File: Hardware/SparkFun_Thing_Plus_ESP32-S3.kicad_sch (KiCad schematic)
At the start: 35 parts, among them J1 USB_C_Receptacle, SW1 4.6x2.8mm, SW2 4.6x2.8mm, U10 ThingPlus, U2 TVS_ESD_USB, U3 ESP32-S3-MINI, U6 AP2112K-3.3

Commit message: Update rev number
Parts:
- R7: PROD_ID RES-14883 -> RES-15187
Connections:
- net +3.3V renamed 3.3V
- net +5V renamed 5V

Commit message: Updates post review
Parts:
- U6: value AP2112K-3.3 -> RT9080-3.3; symbol SparkFun-Regulator:AP2112K-3.3 -> SparkFun-Regulator:RT9080-3.3; Imax (none) -> 600mA; Iq (none) -> 4µA; PROD_ID VREG-12457 -> VREG-19034; VMax (none) -> 6V
- renumbered JP4 to PWR1
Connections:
- net ESP35/~{ALRT}: now reaches U3.31 (IO35)
- net 5V renamed VIN
- net ESP41/NC renamed ESP41/LP_CTL
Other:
- note added: "Differential Pair Calculation Copper Thickness (1oz): 1.4mil/0.035mm Board thickness: 1.6mm Dielectric thickness (layer 1 to 2): 7.9mil/0.2mm Er: 4.6 Trace Spacing: 6mil/0.1524mm Required Trace Width: 9mil/0.2286mm Source: Saturn PCB Toolkit"
- note added: "For modules with ordering codes ending with -N4R2, IO26 connects to the embedded PSRAM and is not available for other uses."
- note added: "IO3: JTAG Signal Source. GPIO by default."
- note removed: "In module variants that have embedded OSPI PSRAM, i.e., that embed ESP32-S3R8, pins IO35, IO36, and IO37 connect to the OSPI PSRAM and are not available for other uses."
- moved on the sheet: C1, C3, C7, D1, R1, R7, SW1, SW2, TP2

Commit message: Add default on to Qwiic power.
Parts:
- JP1: renamed from PWR1; value ~ -> PWR
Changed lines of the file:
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@@
   (symbol (lib_id "SparkFun-Jumper:SolderJumper_2_Bridged") (at 186.69 34.29 90) (unit 1)
     (in_bom yes) (on_board yes) (dnp no) (fields_autoplaced)
-    (property "Reference" "PWR1" (at 184.658 34.29 0)
+    (property "Reference" "JP1" (at 184.658 34.29 0)
       (effects (font (size 1.27 1.27)))
     )
-    (property "Value" "~" (at 189.23 34.29 0)
+    (property "Value" "PWR" (at 189.23 34.29 0)
       (effects (font (size 1.27 1.27)))
     )
@@
       (project "SparkFun_Thing_Plus_ESP32-S3"
         (path "/e3dd3ae4-244d-4cba-9cca-5d2abf83f29a"
-          (reference "PWR1") (unit 1)
+          (reference "JP1") (unit 1)
         )
       )

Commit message: Revise layout post design review
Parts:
- C10: value 1.0uF -> 2.2uF; symbol SparkFun-Capacitor:1.0uF_0402_16V_10% -> SparkFun-Capacitor:2.2uF_0402_10V_10%; PROD_ID CAP-14969 -> CAP-14232; Voltage 16V -> 10V
- SW1, SW2: footprint SparkFun-Switch:Momentary_SMD_4.6x2.8mm -> SparkFun-Switch:Momentary_SMD_4.6x2.8mm_h2.5mm; symbol SparkFun-Switch:SPST_Momentary_4.6x2.8mm -> SparkFun-Switch:SPST_Momentary_SMD_4.6x2.8mm_h2.5mm
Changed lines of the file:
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@@
     )
   )
-  (symbol (lib_id "SparkFun-Switch:SPST_Momentary_4.6x2.8mm") (at 36.83 101.6 270) (unit 1)
+  (symbol (lib_id "SparkFun-Switch:SPST_Momentary_SMD_4.6x2.8mm_h2.5mm") (at 36.83 101.6 270) (unit 1)
     (in_bom yes) (on_board yes) (dnp no) (fields_autoplaced)
     (property "Reference" "SW1" (at 39.37 100.33 90)
@@
       (effects (font (size 1.27 1.27)) (justify left))
     )
-    (property "Footprint" "SparkFun-Switch:Momentary_SMD_4.6x2.8mm" (at 31.75 101.6 0)
-      (effects (font (size 1.27 1.27)) hide)
-    )
-    (property "Datasheet" "~" (at 36.83 101.6 0)
+    (property "Footprint" "SparkFun-Switch:Momentary_SMD_4.6x2.8mm_h2.5mm" (at 31.75 101.6 0)
+      (effects (font (size 1.27 1.27)) hide)
+    )
+    (property "Datasheet" "~" (at 26.67 101.6 0)
       (effects (font (size 1.27 1.27)) hide)
     )
@@
     )
   )
-  (symbol (lib_id "SparkFun-Capacitor:1.0uF_0402_16V_10%") (at 133.35 52.07 0) (unit 1)
+  (symbol (lib_id "SparkFun-Capacitor:2.2uF_0402_10V_10%") (at 133.35 52.07 0) (unit 1)
     (in_bom yes) (on_board yes) (dnp no) (fields_autoplaced)
     (property "Reference" "C10" (at 137.16 48.26 0)
       (effects (font (size 1.27 1.27)) (justify left))
     )
-    (property "Value" "1.0uF" (at 137.16 50.8 0)
+    (property "Value" "2.2uF" (at 137.16 50.8 0)
       (effects (font (size 1.27 1.27)) (justify left))
     )
@@
       (effects (font (size 1.27 1.27)) hide)
     )
-    (property "Datasheet" "https://cdn.sparkfun.com/assets/8/a/4/a/5/Kemet_Capacitor_Datasheet.pdf" (at 133.35 66.04 0)
-      (effects (font (size 1.27 1.27)) hide)
-    )
-    (property "PROD_ID" "CAP-14969" (at 132.08 68.58 0)
-      (effects (font (size 1.27 1.27)) hide)
-    )
-    (property "Voltage" "16V" (at 137.16 53.34 0)
+    (property "Datasheet" "https://cdn.sparkfun.com/assets/8/a/4/a/5/Kemet_Capacitor_Datasheet.pdf" (at 134.62 68.58 0)
+      (effects (font (size 1.27 1.27)) hide)
+    )
+    (property "PROD_ID" "CAP-14232" (at 132.08 66.04 0)
+      (effects (font (size 1.27 1.27)) hide)
+    )
+    (property "Voltage" "10V" (at 137.16 53.34 0)
       (effects (font (size 1.27 1.27)) (justify left))
     )
@@
     )
   )
-  (symbol (lib_id "SparkFun-Switch:SPST_Momentary_4.6x2.8mm") (at 35.56 148.59 270) (unit 1)
+  (symbol (lib_id "SparkFun-Switch:SPST_Momentary_SMD_4.6x2.8mm_h2.5mm") (at 35.56 148.59 270) (unit 1)
     (in_bom yes) (on_board yes) (dnp no) (fields_autoplaced)
     (property "Reference" "SW2" (at 38.1 147.32 90)
@@
       (effects (font (size 1.27 1.27)) (justify left))
     )
-    (property "Footprint" "SparkFun-Switch:Momentary_SMD_4.6x2.8mm" (at 30.48 148.59 0)
-      (effects (font (size 1.27 1.27)) hide)
-    )
-    (property "Datasheet" "~" (at 35.56 148.59 0)
-      (effects (font (size 1.27 1.27)) hide)
-    )
+    (property "Footprint" "SparkFun-Switch:Momentary_SMD_4.6x2.8mm_h2.5mm" (at 30.48 148.59 0)
+      (effects (font (size 1.27 1.27)) hide)
+    )
+    (property "Datasheet" "~" (at 25.4 148.59 0)
+      (effects (font (size 1.27 1.27)) hide)
+    )

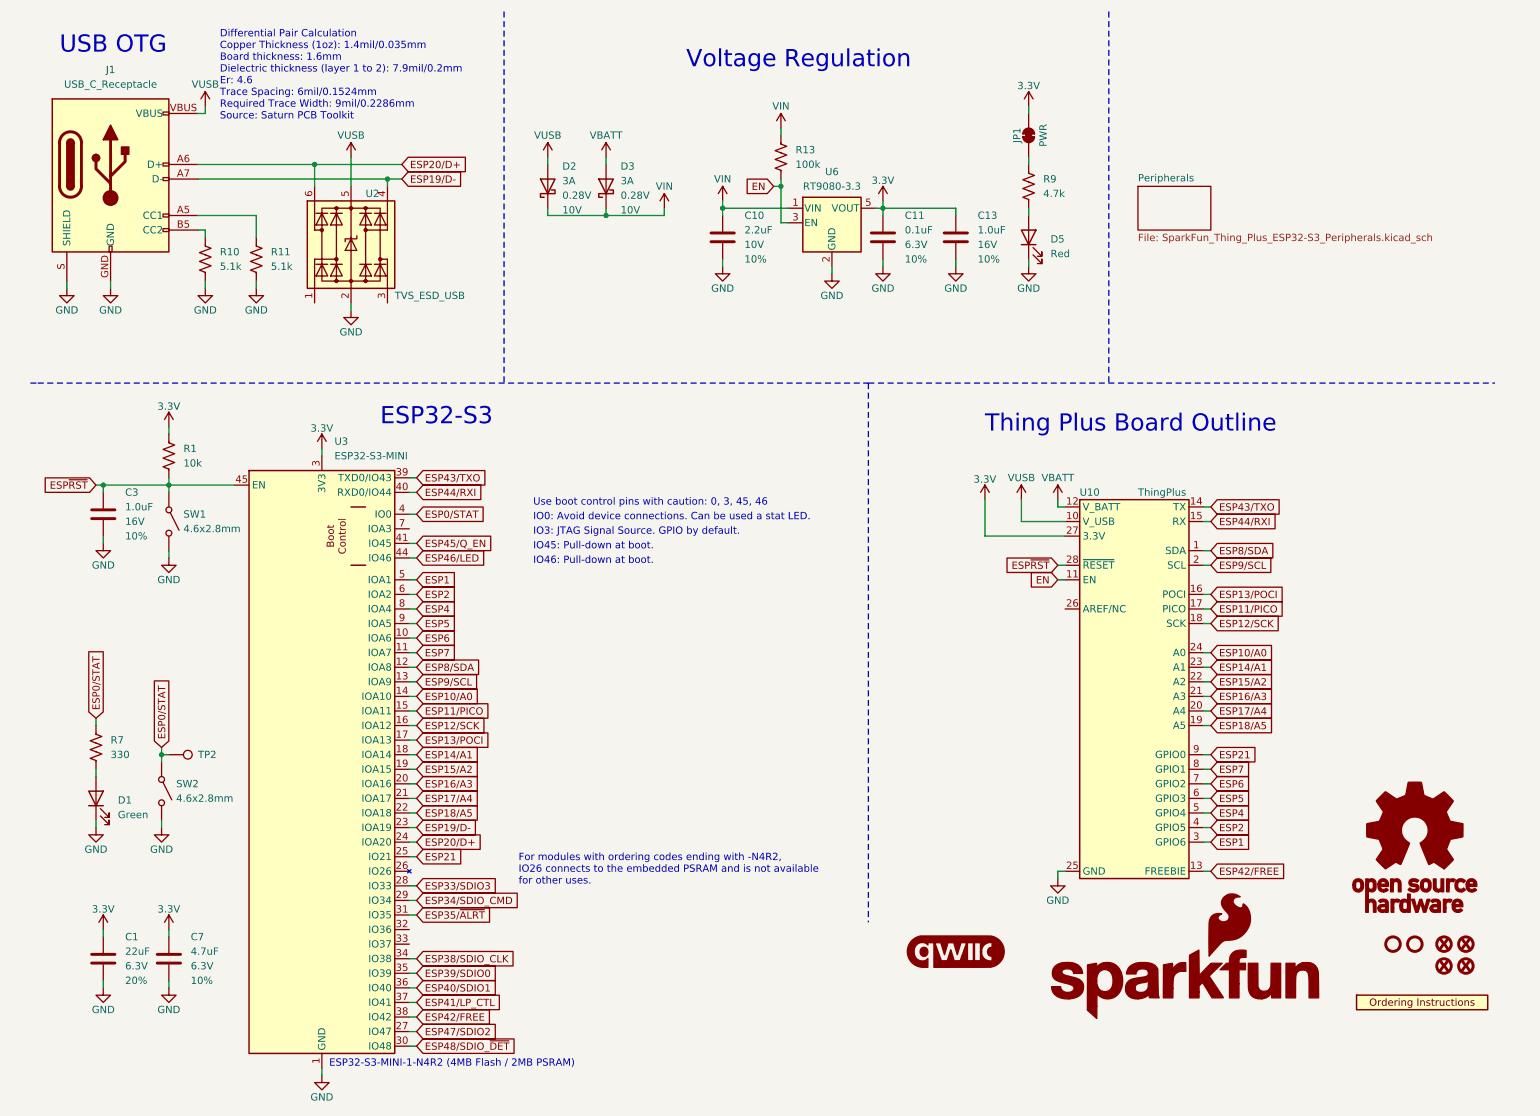
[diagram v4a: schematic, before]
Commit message: Fix 330 prod ID. Update parts to new naming conventions
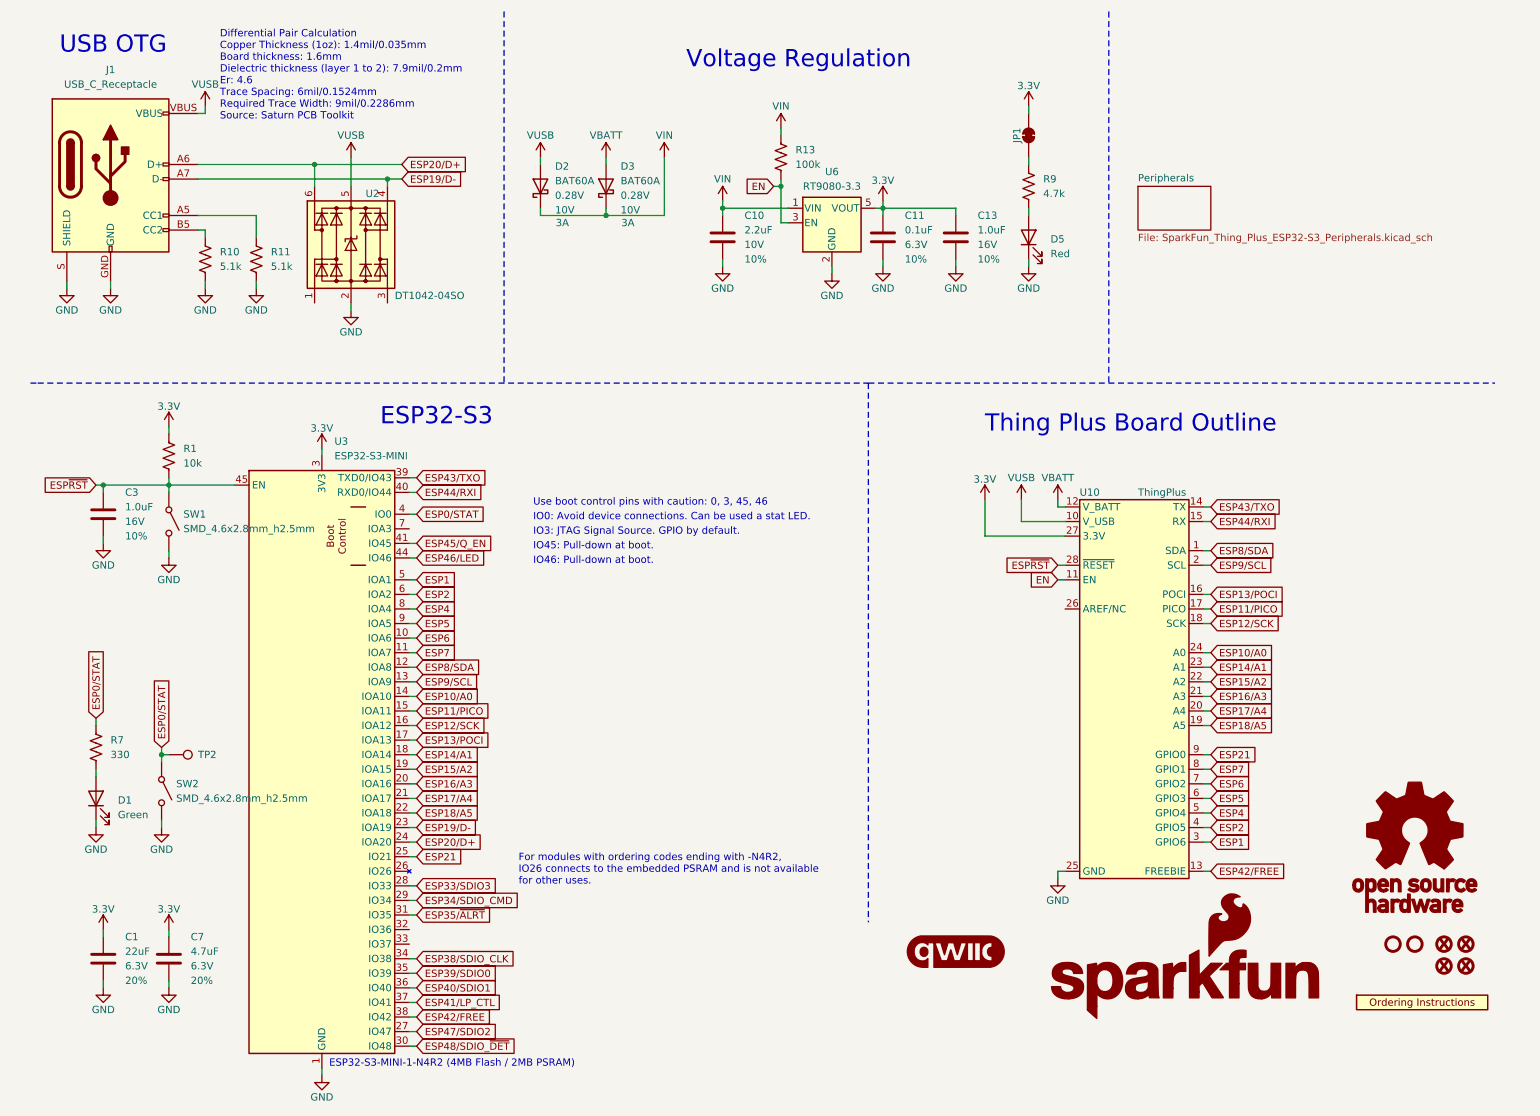
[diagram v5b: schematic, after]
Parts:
- C7: Tolerance 10% -> 20%
- D2, D3: value 3A -> BAT60A; IMax (none) -> 3A
- FID1, FID2, FID3, FID4: value Fiducial_0.5 -> Fiducial_0.5mm
- J1: footprint SparkFun-Connector:USB-C-16P -> SparkFun-Connector:USB-C_16
- JP1: value PWR -> ~; footprint SparkFun-Jumper:SMT-JUMPER_2_NC_TRACE_SILK -> SparkFun-Jumper:Jumper_2_NC_Trace
- R7: PROD_ID RES-15187 -> RES-15407
- ST1, ST3: value Stand_off -> Standoff; footprint SparkFun-Hardware:STAND-OFF -> SparkFun-Hardware:Standoff; symbol SparkFun-Hardware:Stand_off -> SparkFun-Hardware:Standoff
- SW1, SW2: value 4.6x2.8mm -> SMD_4.6x2.8mm_h2.5mm
- U2: value TVS_ESD_USB -> DT1042-04SO
- U9: footprint SparkFun-Aesthetic:ORDERING_INSTRUCTIONS -> SparkFun-Aesthetic:Ordering_Instructions
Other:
- moved on the sheet: D2

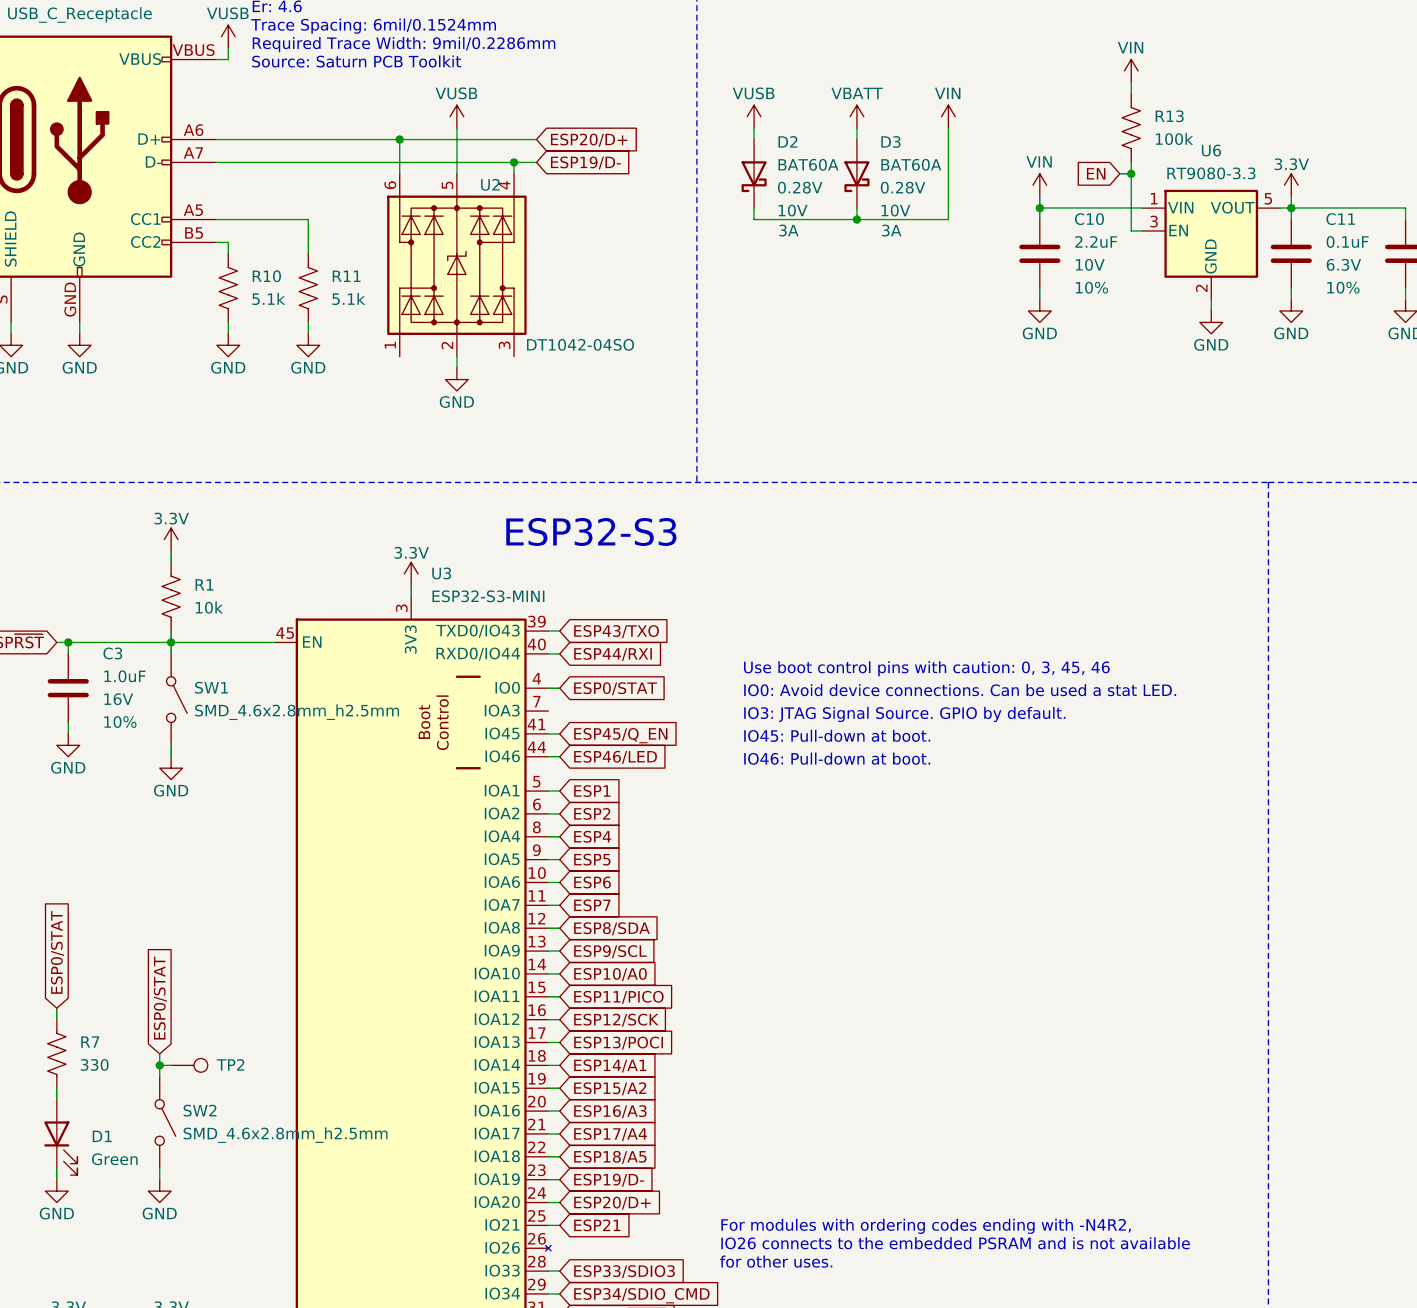
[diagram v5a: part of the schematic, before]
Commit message: Update with current models and symbols
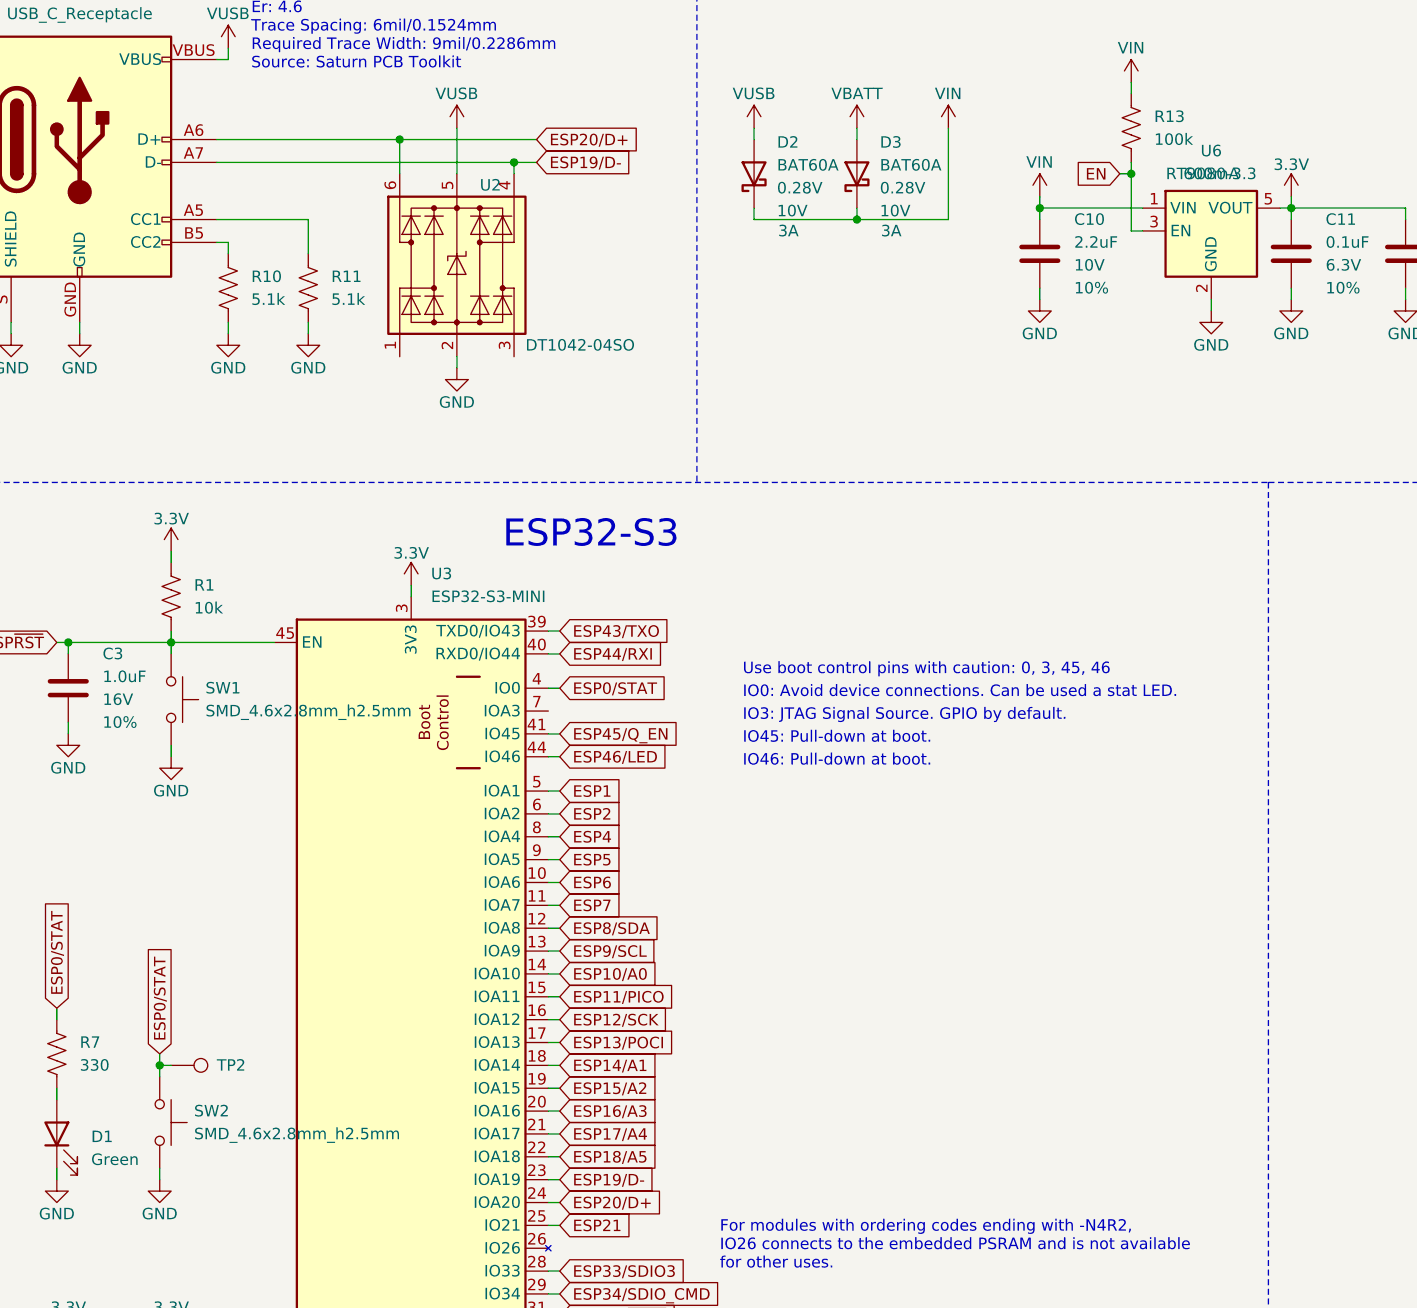
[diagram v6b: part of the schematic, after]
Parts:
- D1: footprint SparkFun-LED:LED_0603_1608Metric -> SparkFun-LED:LED_0603_1608Metric_Green
- D5: footprint SparkFun-LED:LED_0603_1608Metric -> SparkFun-LED:LED_0603_1608Metric_Red
- SW1, SW2: footprint SparkFun-Switch:Momentary_SMD_4.6x2.8mm_h2.5mm -> SparkFun-Switch:Push_SMD_4.6x2.8mm_h2.5mm; symbol SparkFun-Switch:SPST_Momentary_SMD_4.6x2.8mm_h2.5mm -> SparkFun-Switch:SPST_Push_SMD_4.6x2.8mm_h2.5mm
- U6: IMax (none) -> 600mA; VMax 6V -> 5.5V
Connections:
- net at J1.A8 (NC): no longer J1.B8 (NC)
- now unconnected: J1.NC1 (NC), J1.NC2 (NC), J1.NC3 (NC)
